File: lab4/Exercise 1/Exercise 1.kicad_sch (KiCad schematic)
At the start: 6 parts, among them J1(V1,9V) Conn_01x02_Male, SW1 SW_SPDT

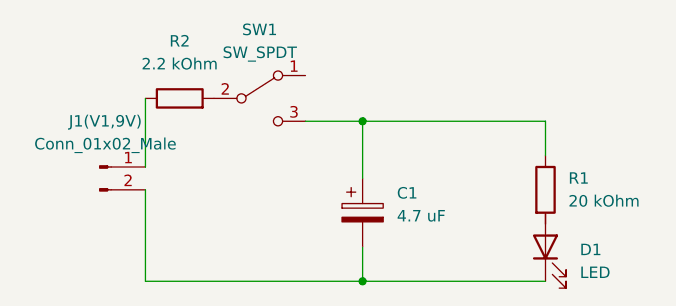
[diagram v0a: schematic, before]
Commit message: added PCB of the SCH
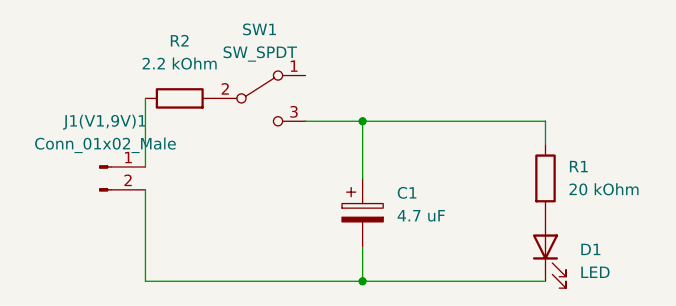
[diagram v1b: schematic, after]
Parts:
- C1: footprint (none) -> Capacitor_THT:C_Radial_D5.0mm_H5.0mm_P2.00mm
- D1: footprint (none) -> LED_THT:LED_D5.0mm
- J1(V1,9V)1: renamed from J1(V1,9V); footprint (none) -> Connector_JST:JST_PH_B2B-PH-K_1x02_P2.00mm_Vertical
- R1, R2: footprint (none) -> Resistor_THT:R_Axial_DIN0516_L15.5mm_D5.0mm_P20.32mm_Horizontal
- SW1: footprint (none) -> Button_Switch_THT:SW_E-Switch_EG1224_SPDT_Angled
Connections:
- net at D1.2 (A): now also R1.2
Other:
- moved on the sheet: R1
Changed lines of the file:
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@@
     (stroke (width 0) (type default) (color 0 0 0 0))
   )
-  (wire (pts (xy 146.05 78.74) (xy 146.05 82.55))
+  (wire (pts (xy 146.05 78.74) (xy 146.05 81.28))
     (stroke (width 0) (type default) (color 0 0 0 0))
   )
@@
     (property "Reference" "R2" (id 0) (at 105.41 69.85 90))
     (property "Value" "2.2 kOhm" (id 1) (at 105.41 72.39 90))
-    (property "Footprint" "" (id 2) (at 105.41 77.978 90)
+    (property "Footprint" "Resistor_THT:R_Axial_DIN0516_L15.5mm_D5.0mm_P20.32mm_Horizontal" (id 2) (at 105.41 77.978 90)
       (effects (font (size 1.27 1.27)) hide)
     )
@@
   (symbol (lib_id "Connector:Conn_01x02_Male") (at 96.52 83.82 0) (unit 1)
     (in_bom yes) (on_board yes) (fields_autoplaced)
-    (property "Reference" "J1(V1,9V)" (id 0) (at 97.155 78.74 0))
+    (property "Reference" "J1(V1,9V)1" (id 0) (at 97.155 78.74 0))
     (property "Value" "Conn_01x02_Male" (id 1) (at 97.155 81.28 0))
-    (property "Footprint" "" (id 2) (at 96.52 83.82 0)
+    (property "Footprint" "Connector_JST:JST_PH_B2B-PH-K_1x02_P2.00mm_Vertical" (id 2) (at 96.52 83.82 0)
       (effects (font (size 1.27 1.27)) hide)
     )
@@
     (property "Reference" "SW1" (id 0) (at 114.3 68.58 0))
     (property "Value" "SW_SPDT" (id 1) (at 114.3 71.12 0))
-    (property "Footprint" "" (id 2) (at 114.3 76.2 0)
+    (property "Footprint" "Button_Switch_THT:SW_E-Switch_EG1224_SPDT_Angled" (id 2) (at 114.3 76.2 0)
       (effects (font (size 1.27 1.27)) hide)
     )
@@
       (effects (font (size 1.27 1.27)) (justify right))
     )
-    (property "Footprint" "" (id 2) (at 146.05 92.71 0)
+    (property "Footprint" "LED_THT:LED_D5.0mm" (id 2) (at 146.05 92.71 0)
       (effects (font (size 1.27 1.27)) hide)
     )
@@
     (pin "2")
   )
-  (symbol (lib_id "Device:R") (at 146.05 86.36 0) (unit 1)
+  (symbol (lib_id "Device:R") (at 146.05 85.09 0) (unit 1)
     (in_bom yes) (on_board yes) (fields_autoplaced)
-    (property "Reference" "R1" (id 0) (at 148.59 85.0899 0)
+    (property "Reference" "R1" (id 0) (at 148.59 83.8199 0)
       (effects (font (size 1.27 1.27)) (justify left))
     )
-    (property "Value" "20 kOhm" (id 1) (at 148.59 87.6299 0)
+    (property "Value" "20 kOhm" (id 1) (at 148.59 86.3599 0)
       (effects (font (size 1.27 1.27)) (justify left))
     )
-    (property "Footprint" "" (id 2) (at 144.272 86.36 90)
+    (property "Footprint" "Resistor_THT:R_Axial_DIN0516_L15.5mm_D5.0mm_P20.32mm_Horizontal" (id 2) (at 144.272 85.09 90)
       (effects (font (size 1.27 1.27)) hide)
     )
-    (property "Datasheet" "~" (id 3) (at 146.05 86.36 0)
+    (property "Datasheet" "~" (id 3) (at 146.05 85.09 0)
       (effects (font (size 1.27 1.27)) hide)
     )
@@
       (effects (font (size 1.27 1.27)) (justify left))
     )
-    (property "Footprint" "" (id 2) (at 126.6952 92.71 0)
+    (property "Footprint" "Capacitor_THT:C_Radial_D5.0mm_H5.0mm_P2.00mm" (id 2) (at 126.6952 92.71 0)
       (effects (font (size 1.27 1.27)) hide)
     )
@@
   (symbol_instances
     (path "/fc6ba860-dc9a-43e7-89cb-5ca45c4efa46"
-      (reference "C1") (unit 1) (value "4.7 uF") (footprint "")
+      (reference "C1") (unit 1) (value "4.7 uF") (footprint "Capacitor_THT:C_Radial_D5.0mm_H5.0mm_P2.00mm")
     )
     (path "/5b063abb-debb-47bc-97ee-08f816d68c25"
-      (reference "D1") (unit 1) (value "LED") (footprint "")
+      (reference "D1") (unit 1) (value "LED") (footprint "LED_THT:LED_D5.0mm")
     )
     (path "/0db99e8e-aa88-46d3-874b-9458e967a432"
-      (reference "J1(V1,9V)") (unit 1) (value "Conn_01x02_Male") (footprint "")
+      (reference "J1(V1,9V)1") (unit 1) (value "Conn_01x02_Male") (footprint "Connector_JST:JST_PH_B2B-PH-K_1x02_P2.00mm_Vertical")
     )
     (path "/70348e5a-6458-41a5-a693-b593a013e223"
-      (reference "R1") (unit 1) (value "20 kOhm") (footprint "")
+      (reference "R1") (unit 1) (value "20 kOhm") (footprint "Resistor_THT:R_Axial_DIN0516_L15.5mm_D5.0mm_P20.32mm_Horizontal")
     )
     (path "/0d202b14-87d0-4e2d-8adf-fdeca92d2ddf"
-      (reference "R2") (unit 1) (value "2.2 kOhm") (footprint "")
+      (reference "R2") (unit 1) (value "2.2 kOhm") (footprint "Resistor_THT:R_Axial_DIN0516_L15.5mm_D5.0mm_P20.32mm_Horizontal")
     )
     (path "/5931f120-c694-4aae-b706-1fbaa187836e"
-      (reference "SW1") (unit 1) (value "SW_SPDT") (footprint "")
+      (reference "SW1") (unit 1) (value "SW_SPDT") (footprint "Button_Switch_THT:SW_E-Switch_EG1224_SPDT_Angled")
     )
   )
